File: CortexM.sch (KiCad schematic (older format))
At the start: 25 parts, among them J1 USB_B_Micro, J2 Conn_01x15, J3 Conn_01x15, U1 XC6206PxxxMR, U2 STM32F103C8Tx, Y1 8MHz

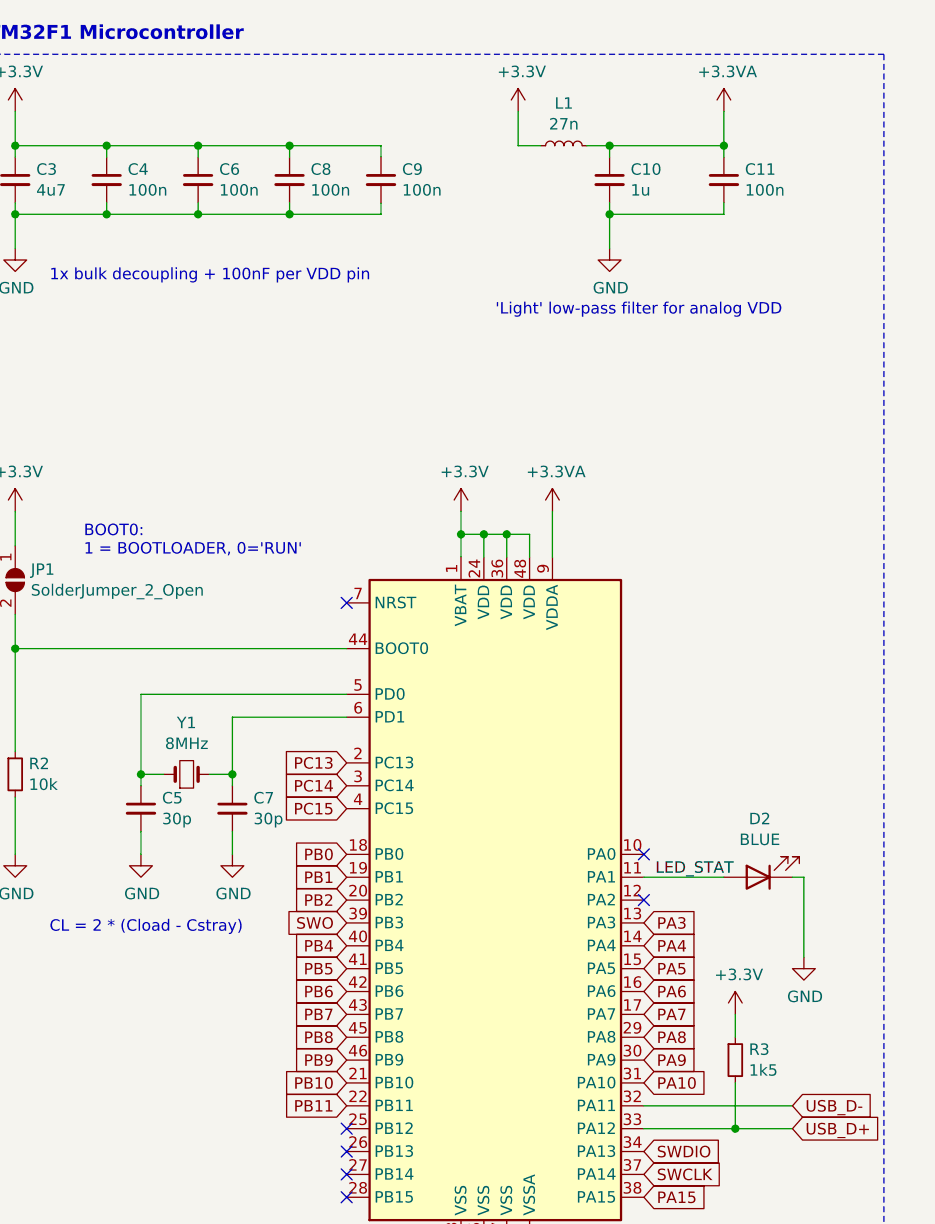
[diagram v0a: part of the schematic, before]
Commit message: Added capacitor footprints
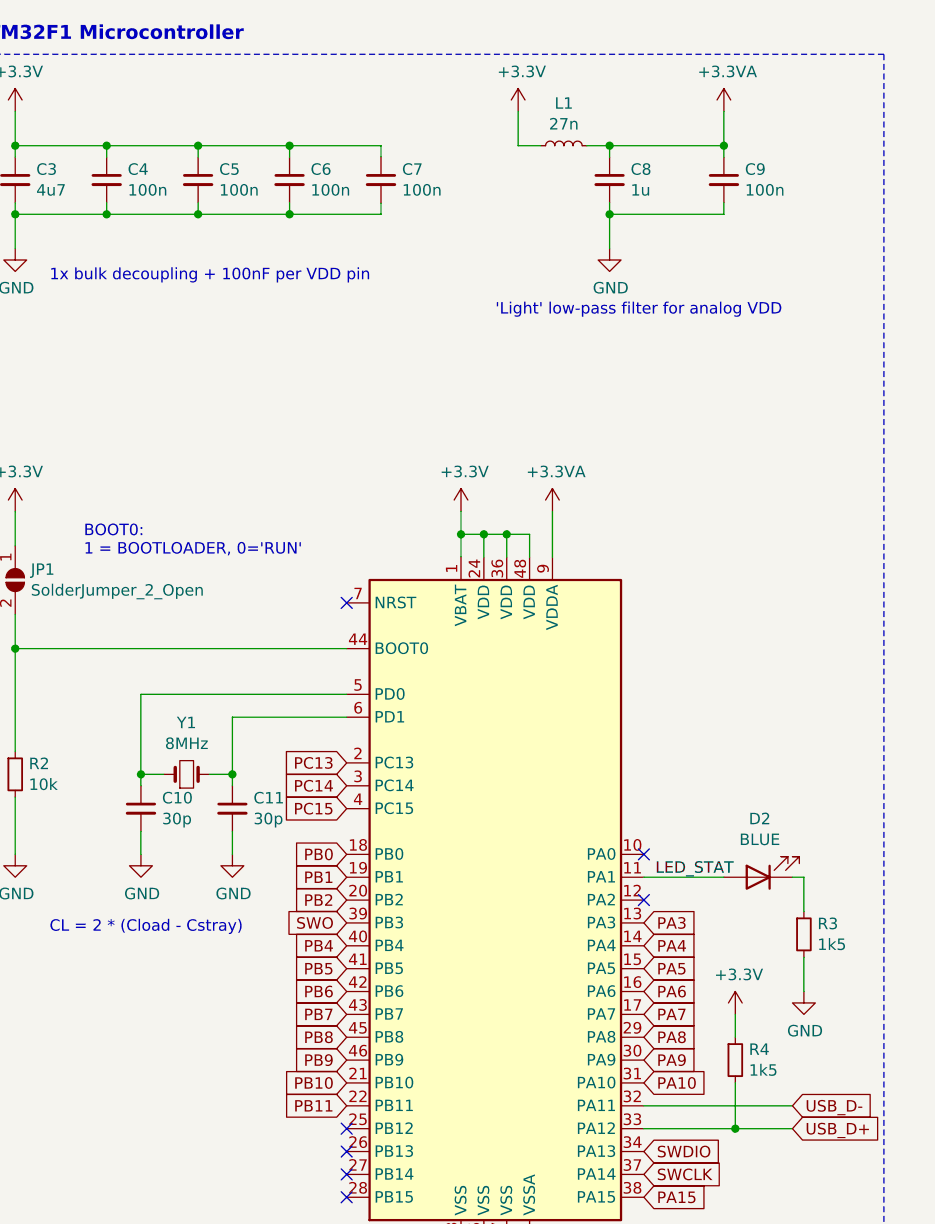
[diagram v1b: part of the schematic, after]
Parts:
- added R3: 1k5, symbol Device:R_Small
- C1, C2, C3: footprint (none) -> Capacitor_SMD:C_0603_1608Metric
- C10: renamed from C5; footprint (none) -> Capacitor_SMD:C_0402_1005Metric
- C11: renamed from C7; footprint (none) -> Capacitor_SMD:C_0402_1005Metric
- C4: footprint (none) -> Capacitor_SMD:C_0402_1005Metric
- C5: renamed from C6; footprint (none) -> Capacitor_SMD:C_0402_1005Metric
- C6: renamed from C8; footprint (none) -> Capacitor_SMD:C_0402_1005Metric
- C7: renamed from C9; footprint (none) -> Capacitor_SMD:C_0402_1005Metric
- C8: renamed from C10; footprint (none) -> Capacitor_SMD:C_0402_1005Metric
- C9: renamed from C11; footprint (none) -> Capacitor_SMD:C_0402_1005Metric
- renumbered R3 to R4
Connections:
- net GND: now also R3.2; no longer D2.1 (K)
- new net: D2.1 (K), R3.1
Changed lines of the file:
@@
 F 0 "C1" H 1550 1850 50  0000 L CNN
 F 1 "1u" H 1550 1750 50  0000 L CNN
-F 2 "" H 1750 1800 50  0001 C CNN
+F 2 "Capacitor_SMD:C_0603_1608Metric" H 1750 1800 50  0001 C CNN
 F 3 "~" H 1750 1800 50  0001 C CNN
 	1    1750 1800
@@
 F 0 "C2" H 2542 1846 50  0000 L CNN
 F 1 "1u" H 2550 1750 50  0000 L CNN
-F 2 "" H 2450 1800 50  0001 C CNN
+F 2 "Capacitor_SMD:C_0603_1608Metric" H 2450 1800 50  0001 C CNN
 F 3 "~" H 2450 1800 50  0001 C CNN
 	1    2450 1800
@@
 L power:GND #PWR025
 U 1 1 5FC229C5
-P 10750 4650
-F 0 "#PWR025" H 10750 4400 50  0001 C CNN
-F 1 "GND" H 10755 4477 50  0000 C CNN
-F 2 "" H 10750 4650 50  0001 C CNN
-F 3 "" H 10750 4650 50  0001 C CNN
-	1    10750 4650
+P 10750 4800
+F 0 "#PWR025" H 10750 4550 50  0001 C CNN
+F 1 "GND" H 10755 4627 50  0000 C CNN
+F 2 "" H 10750 4800 50  0001 C CNN
+F 3 "" H 10750 4800 50  0001 C CNN
+	1    10750 4800
 	1    0    0    -1
 $EndComp
@@
 Wire Wire Line
 	10700 4300 10750 4300
-Wire Wire Line
-	10750 4300 10750 4650
 Text Label 10100 4300 0    50   ~ 0
 LED_STAT
@@
 $EndComp
 $Comp
-L Device:R_Small R3
+L Device:R_Small R4
 U 1 1 5FC2B2BA
 P 10450 5100
-F 0 "R3" H 10509 5146 50  0000 L CNN
+F 0 "R4" H 10509 5146 50  0000 L CNN
 F 1 "1k5" H 10509 5055 50  0000 L CNN
 F 2 "" H 10450 5100 50  0001 C CNN
@@
 $EndComp
 $Comp
-L Device:C_Small C5
+L Device:C_Small C10
 U 1 1 5FC32777
 P 7850 4000
-F 0 "C5" H 7942 4046 50  0000 L CNN
+F 0 "C10" H 7942 4046 50  0000 L CNN
 F 1 "30p" H 7942 3955 50  0000 L CNN
-F 2 "" H 7850 4000 50  0001 C CNN
+F 2 "Capacitor_SMD:C_0402_1005Metric" H 7850 4000 50  0001 C CNN
 F 3 "~" H 7850 4000 50  0001 C CNN
 	1    7850 4000
@@
 $EndComp
 $Comp
-L Device:C_Small C7
+L Device:C_Small C11
 U 1 1 5FC33280
 P 8250 4000
-F 0 "C7" H 8342 4046 50  0000 L CNN
+F 0 "C11" H 8342 4046 50  0000 L CNN
 F 1 "30p" H 8342 3955 50  0000 L CNN
-F 2 "" H 8250 4000 50  0001 C CNN
+F 2 "Capacitor_SMD:C_0402_1005Metric" H 8250 4000 50  0001 C CNN
 F 3 "~" H 8250 4000 50  0001 C CNN
 	1    8250 4000
@@
 F 0 "C3" H 7392 1296 50  0000 L CNN
 F 1 "4u7" H 7392 1205 50  0000 L CNN
-F 2 "" H 7300 1250 50  0001 C CNN
+F 2 "Capacitor_SMD:C_0603_1608Metric" H 7300 1250 50  0001 C CNN
 F 3 "~" H 7300 1250 50  0001 C CNN
 	1    7300 1250
@@
 F 0 "C4" H 7792 1296 50  0000 L CNN
 F 1 "100n" H 7792 1205 50  0000 L CNN
-F 2 "" H 7700 1250 50  0001 C CNN
+F 2 "Capacitor_SMD:C_0402_1005Metric" H 7700 1250 50  0001 C CNN
 F 3 "~" H 7700 1250 50  0001 C CNN
 	1    7700 1250
@@
 $EndComp
 $Comp
-L Device:C_Small C6
+L Device:C_Small C5
 U 1 1 5FC4B8EF
 P 8100 1250
-F 0 "C6" H 8192 1296 50  0000 L CNN
+F 0 "C5" H 8192 1296 50  0000 L CNN
 F 1 "100n" H 8192 1205 50  0000 L CNN
-F 2 "" H 8100 1250 50  0001 C CNN
+F 2 "Capacitor_SMD:C_0402_1005Metric" H 8100 1250 50  0001 C CNN
 F 3 "~" H 8100 1250 50  0001 C CNN
 	1    8100 1250
@@
 $EndComp
 $Comp
-L Device:C_Small C8
+L Device:C_Small C6
 U 1 1 5FC4BC1B
 P 8500 1250
-F 0 "C8" H 8592 1296 50  0000 L CNN
+F 0 "C6" H 8592 1296 50  0000 L CNN
 F 1 "100n" H 8592 1205 50  0000 L CNN
-F 2 "" H 8500 1250 50  0001 C CNN
+F 2 "Capacitor_SMD:C_0402_1005Metric" H 8500 1250 50  0001 C CNN
 F 3 "~" H 8500 1250 50  0001 C CNN
 	1    8500 1250
@@
 $EndComp
 $Comp
-L Device:C_Small C9
+L Device:C_Small C7
 U 1 1 5FC4C042
 P 8900 1250
-F 0 "C9" H 8992 1296 50  0000 L CNN
+F 0 "C7" H 8992 1296 50  0000 L CNN
 F 1 "100n" H 8992 1205 50  0000 L CNN
-F 2 "" H 8900 1250 50  0001 C CNN
+F 2 "Capacitor_SMD:C_0402_1005Metric" H 8900 1250 50  0001 C CNN
 F 3 "~" H 8900 1250 50  0001 C CNN
 	1    8900 1250
@@
 $EndComp
 $Comp
-L Device:C_Small C10
+L Device:C_Small C8
 U 1 1 5FC5FBCC
 P 9900 1250
-F 0 "C10" H 9992 1296 50  0000 L CNN
+F 0 "C8" H 9992 1296 50  0000 L CNN
 F 1 "1u" H 9992 1205 50  0000 L CNN
-F 2 "" H 9900 1250 50  0001 C CNN
+F 2 "Capacitor_SMD:C_0402_1005Metric" H 9900 1250 50  0001 C CNN
 F 3 "~" H 9900 1250 50  0001 C CNN
 	1    9900 1250
@@
 $EndComp
 $Comp
-L Device:C_Small C11
+L Device:C_Small C9
 U 1 1 5FC6028C
 P 10400 1250
-F 0 "C11" H 10492 1296 50  0000 L CNN
+F 0 "C9" H 10492 1296 50  0000 L CNN
 F 1 "100n" H 10492 1205 50  0000 L CNN
-F 2 "" H 10400 1250 50  0001 C CNN
+F 2 "Capacitor_SMD:C_0402_1005Metric" H 10400 1250 50  0001 C CNN
 F 3 "~" H 10400 1250 50  0001 C CNN
 	1    10400 1250
@@
 Text Notes 8300 650  2    61   ~ 12
 STM32F1 Microcontroller
+$Comp
+L Device:R_Small R3
+U 1 1 5FD2F348
+P 10750 4550
+F 0 "R3" H 10809 4596 50  0000 L CNN
+F 1 "1k5" H 10809 4505 50  0000 L CNN
+F 2 "" H 10750 4550 50  0001 C CNN
+F 3 "~" H 10750 4550 50  0001 C CNN
+	1    10750 4550
+	1    0    0    -1
+$EndComp
+Wire Wire Line
+	10750 4450 10750 4300
+Wire Wire Line
+	10750 4800 10750 4650
 $EndSCHEMATC

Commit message: finished footprint assignment
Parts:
- D1, D2: footprint (none) -> LED_SMD:LED_0603_1608Metric
- FB1: footprint (none) -> Inductor_SMD:L_0805_2012Metric
- J1: footprint (none) -> Connector_USB:USB_Micro-B_Wuerth_629105150521
- J2, J3: footprint (none) -> Connector_PinHeader_2.54mm:PinHeader_1x15_P2.54mm_Vertical
- JP1: footprint (none) -> Jumper:SolderJumper-2_P1.3mm_Open_Pad1.0x1.5mm
- L1: footprint (none) -> Inductor_SMD:L_0402_1005Metric
- R1, R3: footprint (none) -> Resistor_SMD:R_0603_1608Metric
- R2, R4: footprint (none) -> Resistor_SMD:R_0402_1005Metric
- Y1: footprint (none) -> Crystal:Crystal_SMD_5032-2Pin_5.0x3.2mm
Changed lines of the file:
@@
 F 0 "J1" H 907 1817 50  0000 C CNN
 F 1 "USB_B_Micro" H 907 1726 50  0000 C CNN
-F 2 "" H 1000 1300 50  0001 C CNN
+F 2 "Connector_USB:USB_Micro-B_Wuerth_629105150521" H 1000 1300 50  0001 C CNN
 F 3 "~" H 1000 1300 50  0001 C CNN
 	1    850  1350
@@
 F 0 "FB1" V 1350 1150 50  0000 C CNN
 F 1 "100R" V 1450 1150 50  0000 C CNN
-F 2 "" V 1530 1150 50  0001 C CNN
+F 2 "Inductor_SMD:L_0805_2012Metric" V 1530 1150 50  0001 C CNN
 F 3 "~" H 1600 1150 50  0001 C CNN
 	1    1600 1150
@@
 F 0 "R1" H 2900 1500 50  0000 L CNN
 F 1 "1k5" H 2900 1400 50  0000 L CNN
-F 2 "" H 3100 1450 50  0001 C CNN
+F 2 "Resistor_SMD:R_0603_1608Metric" H 3100 1450 50  0001 C CNN
 F 3 "~" H 3100 1450 50  0001 C CNN
 	1    3100 1450
@@
 F 0 "D1" H 2893 895 50  0000 C CNN
 F 1 "GREEN" H 2900 1000 50  0000 C CNN
-F 2 "" H 2900 1150 50  0001 C CNN
+F 2 "LED_SMD:LED_0603_1608Metric" H 2900 1150 50  0001 C CNN
 F 3 "~" H 2900 1150 50  0001 C CNN
 	1    2900 1150
@@
 F 0 "D2" H 10543 4045 50  0000 C CNN
 F 1 "BLUE" H 10543 4136 50  0000 C CNN
-F 2 "" H 10550 4300 50  0001 C CNN
+F 2 "LED_SMD:LED_0603_1608Metric" H 10550 4300 50  0001 C CNN
 F 3 "~" H 10550 4300 50  0001 C CNN
 	1    10550 4300
@@
 F 0 "R4" H 10509 5146 50  0000 L CNN
 F 1 "1k5" H 10509 5055 50  0000 L CNN
-F 2 "" H 10450 5100 50  0001 C CNN
+F 2 "Resistor_SMD:R_0402_1005Metric" H 10450 5100 50  0001 C CNN
 F 3 "~" H 10450 5100 50  0001 C CNN
 	1    10450 5100
@@
 F 0 "Y1" H 8050 4075 50  0000 C CNN
 F 1 "8MHz" H 8050 3984 50  0000 C CNN
-F 2 "" H 8050 3850 50  0001 C CNN
+F 2 "Crystal:Crystal_SMD_5032-2Pin_5.0x3.2mm" H 8050 3850 50  0001 C CNN
 F 3 "~" H 8050 3850 50  0001 C CNN
 	1    8050 3850
@@
 F 0 "R2" H 7359 3896 50  0000 L CNN
 F 1 "10k" H 7359 3805 50  0000 L CNN
-F 2 "" H 7300 3850 50  0001 C CNN
+F 2 "Resistor_SMD:R_0402_1005Metric" H 7300 3850 50  0001 C CNN
 F 3 "~" H 7300 3850 50  0001 C CNN
 	1    7300 3850
@@
 F 0 "JP1" V 7254 3068 50  0000 L CNN
 F 1 "SolderJumper_2_Open" V 7345 3068 50  0000 L CNN
-F 2 "" H 7300 3000 50  0001 C CNN
+F 2 "Jumper:SolderJumper-2_P1.3mm_Open_Pad1.0x1.5mm" H 7300 3000 50  0001 C CNN
 F 3 "~" H 7300 3000 50  0001 C CNN
 	1    7300 3000
@@
 F 0 "L1" V 9885 1100 50  0000 C CNN
 F 1 "27n" V 9794 1100 50  0000 C CNN
-F 2 "" H 9700 1100 50  0001 C CNN
+F 2 "Inductor_SMD:L_0402_1005Metric" H 9700 1100 50  0001 C CNN
 F 3 "~" H 9700 1100 50  0001 C CNN
 	1    9700 1100
@@
 F 0 "J2" H 1630 3642 50  0000 L CNN
 F 1 "Conn_01x15" H 1630 3551 50  0000 L CNN
-F 2 "" H 1550 3600 50  0001 C CNN
+F 2 "Connector_PinHeader_2.54mm:PinHeader_1x15_P2.54mm_Vertical" H 1550 3600 50  0001 C CNN
 F 3 "~" H 1550 3600 50  0001 C CNN
 	1    1550 3600
@@
 F 0 "J3" H 2680 3642 50  0000 L CNN
 F 1 "Conn_01x15" H 2680 3551 50  0000 L CNN
-F 2 "" H 2600 3600 50  0001 C CNN
+F 2 "Connector_PinHeader_2.54mm:PinHeader_1x15_P2.54mm_Vertical" H 2600 3600 50  0001 C CNN
 F 3 "~" H 2600 3600 50  0001 C CNN
 	1    2600 3600
@@
 F 0 "R3" H 10809 4596 50  0000 L CNN
 F 1 "1k5" H 10809 4505 50  0000 L CNN
-F 2 "" H 10750 4550 50  0001 C CNN
+F 2 "Resistor_SMD:R_0603_1608Metric" H 10750 4550 50  0001 C CNN
 F 3 "~" H 10750 4550 50  0001 C CNN
 	1    10750 4550
